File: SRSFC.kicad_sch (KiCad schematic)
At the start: 50 parts, among them J1 SWD_interface, X1 25MHz

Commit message: added servo connectors, schema done (probably)
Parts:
- added J2: POWER, Connector_PinHeader_2.54mm:PinHeader_1x02_P2.54mm_Vertical, symbol Connector_Generic:Conn_01x02
- added J3: SERVO1, Connector_PinHeader_2.54mm:PinHeader_1x03_P2.54mm_Vertical, symbol Connector_Generic:Conn_01x03
- added J4: SERVO2, Connector_PinHeader_2.54mm:PinHeader_1x03_P2.54mm_Vertical, symbol Connector_Generic:Conn_01x03
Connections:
- net +3.3V: now also U6.6 (CSB)
- net GND: now also J2.1 (Pin_1), J3.1 (Pin_1), J4.1 (Pin_1)
- net bmp_scl: now reaches U6.2 (SCK)
- net bmp_sda: now reaches U6.4 (SDI)
- net servo_2: now reaches U1.67 (PA8)
- net servo_2: now also J4.3 (Pin_3)
- net servo_1: now reaches U1.92 (PB6)
- net servo_1: now also J3.3 (Pin_3)
- net +5V renamed VCC
- net VCC: now also J2.2 (Pin_2), J3.2 (Pin_2), J4.2 (Pin_2)
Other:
- moved on the sheet: C1, C10, C11, C12, C13, C14, C15, C16, C17, C18, C19, C2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

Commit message: finished v1 (bad) layout)
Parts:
- C27: value .1uF -> 100nF
- R2: value 1k -> 220
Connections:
- net bmp_scl: now also U1.95 (PB8)
- net bmp_sda: now also U1.93 (PB7)
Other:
- title: (none) -> SRS Flight Computer
- moved on the sheet: C18, C19, C20, C21, C26, J1, R3, R4, R5, R6, U3, U4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
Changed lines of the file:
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@@
 	(generator_version "8.0")
 	(paper "A2")
+	(title_block
+		(title "SRS Flight Computer")
+		(date "2024-11-22")
+		(rev "V1")
+	)

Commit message: updated readme
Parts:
- removed C17, C18, C20: 100nF, Capacitor_SMD:C_0402_1005Metric, symbol Device:C
- removed C19, C21: 1uF, Capacitor_SMD:C_0402_1005Metric, symbol Device:C
- removed U2: ~, ICM-20948:QFN-24_L3.0-W3.0-P0.40-BL-EP, symbol ICM-20948:ICM-20948
- removed U3: ~, TXS0108EPWR:TSSOP-20_L6.5-W4.4-P0.65-LS6.4-BL, symbol TXS0108EPWR:TXS0108EPWR
- removed U4: ~, LP5907MFX-1.8:SOT-23-5_L3.0-W1.7-P0.95-LS2.8-BR, symbol LP5907MFX-1.8:LP5907MFX-1.8/NOPB
- added J5: SERVO3, Connector_PinHeader_2.54mm:PinHeader_1x03_P2.54mm_Vertical, symbol Connector_Generic:Conn_01x03
- added J6: SERVO4, Connector_PinHeader_2.54mm:PinHeader_1x03_P2.54mm_Vertical, symbol Connector_Generic:Conn_01x03
- added J7: SERVO5, Connector_PinHeader_2.54mm:PinHeader_1x03_P2.54mm_Vertical, symbol Connector_Generic:Conn_01x03
- added JP1, JP2: address_select, Jumper:SolderJumper-2_P1.3mm_Open_RoundedPad1.0x1.5mm, symbol Jumper:SolderJumper_2_Open
- added R10, R9: 4.7k, Resistor_SMD:R_0402_1005Metric, symbol Device:R
- added R7, R8: 10k, Resistor_SMD:R_0402_1005Metric, symbol Device:R
- added U2: ~, LSM6DSOWTR:LGA-14L_L3.0-W2.5-P0.50-TL, symbol LSM6DSOWTR:LSM6DSOWTR
- C15: value 1uF -> 100nF
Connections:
- net +3.3V: now also C15.2, C16.1, R10.1, R7.2, R8.2, R9.1, U2.5 (VDDIO), U2.8 (VDD)
- net GND: now also C16.2, J5.1 (Pin_1), J6.1 (Pin_1), J7.1 (Pin_1), JP1.2 (B), JP2.2 (B), U2.2 (SDx), U2.3 (SCx), U2.6 (GND), U2.7 (GND); no longer C16.1
- net VCC: now also J5.2 (Pin_2), J6.2 (Pin_2), J7.2 (Pin_2)
- net bmp_scl: now also R10.2, U2.13 (SCL)
- net bmp_sda: now also R9.2, U2.14 (SDA)
- net at U6.5 (SDO): now also JP2.1 (A)
- net servo_3: now reaches U1.63 (PC6)
- net servo_3: now also J5.3 (Pin_3)
- net servo_4: now reaches U1.64 (PC7)
- net servo_4: now also J6.3 (Pin_3)
- net servo_5: now reaches U1.68 (PA9)
- net servo_5: now also J7.3 (Pin_3)
- removed net +1V8: C15.2, C16.2
- net SPI_CS: no longer names the net of U1.77 (PA15)
- net SPI_MISO: no longer names the net of U1.90 (PB4)
- net SPI_MOSI: no longer names the net of U1.88 (PD7)
- net SPI_SCK: no longer names the net of U1.89 (PB3)
- new net: JP1.1 (A), R8.1, U2.1 (SDO/SA0)
- new net: R7.1, U2.12 (CS)
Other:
- moved on the sheet: J2, J3, J4

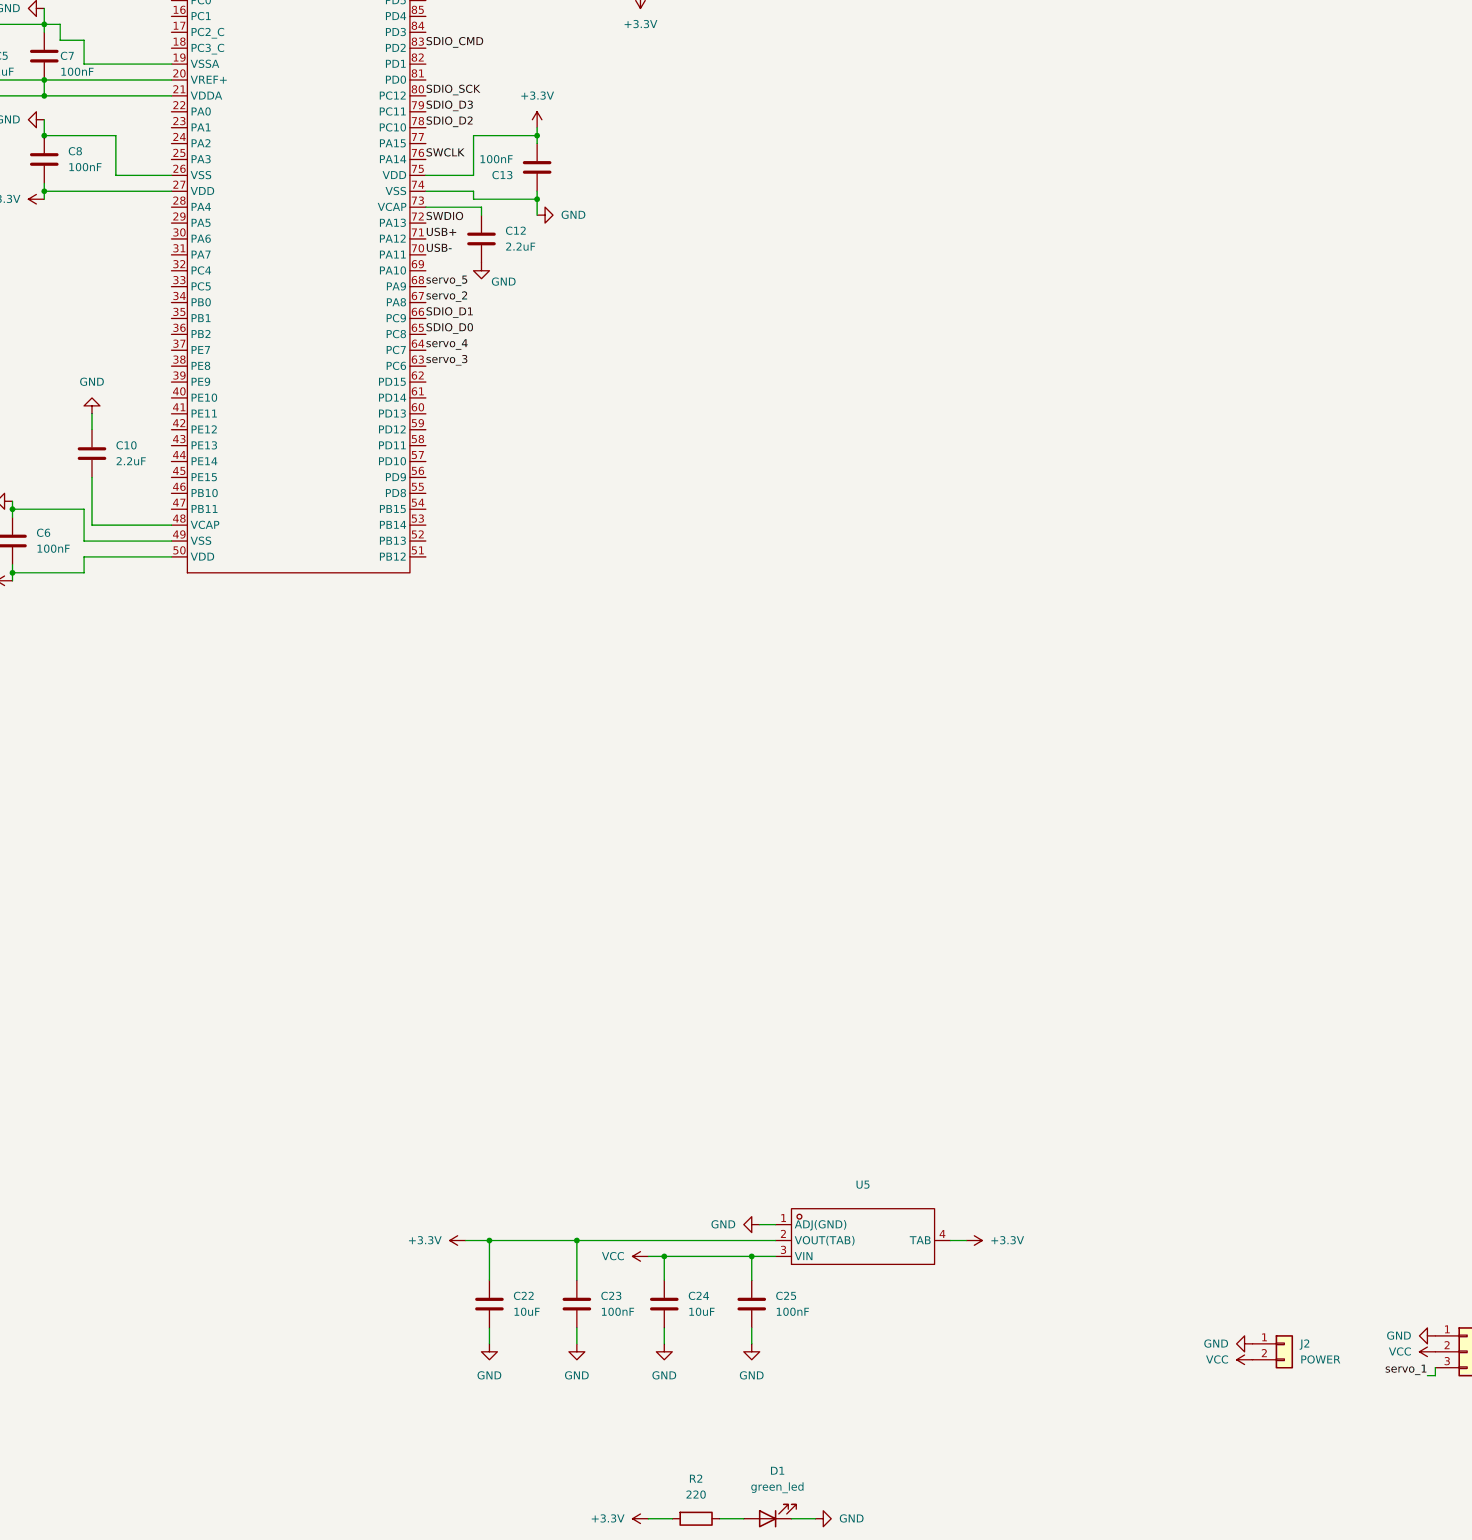
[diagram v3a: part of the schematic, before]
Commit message: added silkscreen, added UART interface
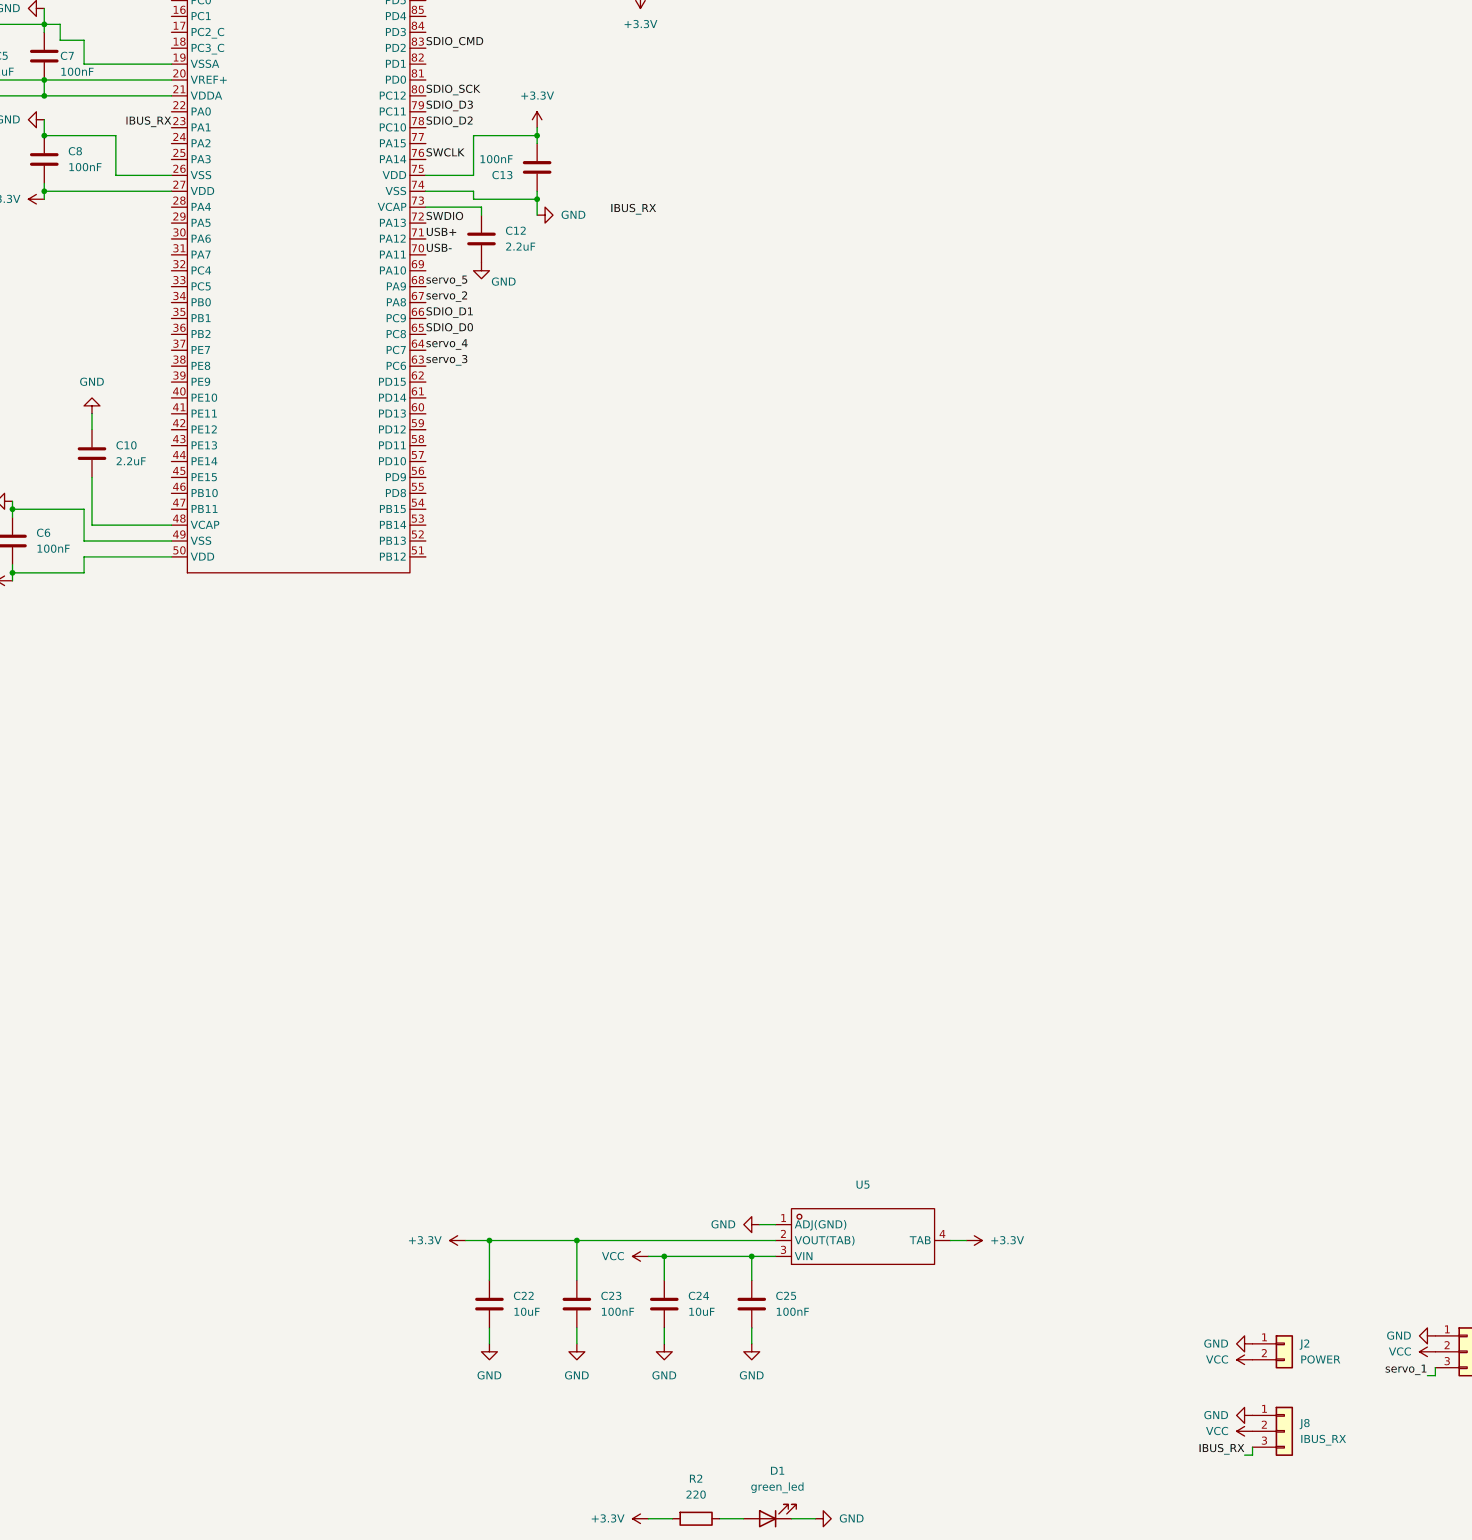
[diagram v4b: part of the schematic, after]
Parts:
- added J8: IBUS_RX, Connector_PinHeader_2.54mm:PinHeader_1x03_P2.54mm_Vertical, symbol Connector_Generic:Conn_01x03
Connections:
- net GND: now also J8.1 (Pin_1)
- net VCC: now also J8.2 (Pin_2)
- net IBUS_RX: now reaches U1.23 (PA1)
- net IBUS_RX: now also J8.3 (Pin_3)

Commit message: changed sensors from i2c to SPI, fixed silkscreen
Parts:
- removed JP1, JP2: address_select, Jumper:SolderJumper-2_P1.3mm_Open_RoundedPad1.0x1.5mm, symbol Jumper:SolderJumper_2_Open
- removed R10, R9: 4.7k, Resistor_SMD:R_0402_1005Metric, symbol Device:R
- removed R7, R8: 10k, Resistor_SMD:R_0402_1005Metric, symbol Device:R
- added C17: 100nF, Capacitor_SMD:C_0402_1005Metric, symbol Device:C
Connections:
- net +3.3V: now also C15.1, C16.2, C17.1; no longer C15.2, C16.1, U6.6 (CSB)
- net GND: now also C15.2, C16.1, C17.2; no longer C15.1, C16.2
- net SPI_MISO_LSM: now reaches U2.1 (SDO/SA0)
- net SPI_MISO_LSM: now also U1.90 (PB4)
- net SPI_CS_LSM: now reaches U2.12 (CS)
- net SPI_CS_LSM: now also U1.88 (PD7)
- net SPI_MISO_BMP: now reaches U6.5 (SDO)
- net SPI_MISO_BMP: now also U1.4 (PE5)
- net SPI_SCK_BMP: now reaches U1.1 (PE2)
- net SPI_SCK_BMP: now also U6.2 (SCK)
- net SPI_CS_BMP: now reaches U1.3 (PE4)
- net SPI_CS_BMP: now also U6.6 (CSB)
- net SPI_MOSI_BMP: now reaches U1.5 (PE6)
- net SPI_MOSI_BMP: now also U6.4 (SDI)
- net SPI_SCK_LSM: now reaches U1.89 (PB3)
- net SPI_SCK_LSM: now also U2.13 (SCL)
- net SPI_MOSI_LSM: now reaches U1.91 (PB5)
- net SPI_MOSI_LSM: now also U2.14 (SDA)
- removed net bmp_scl: U1.95 (PB8), U2.13 (SCL), U6.2 (SCK)
- removed net bmp_sda: U1.93 (PB7), U2.14 (SDA), U6.4 (SDI)
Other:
- moved on the sheet: C11, R1

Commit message: final commit before ordering
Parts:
- R2: value 220 -> 100
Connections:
- net GND: now also CARD1.10, CARD1.11, CARD1.12, CARD1.13, CARD1.6 (VSS); no longer CARD1.CD
- net SDIO_CMD: now also CARD1.3 (CMD); no longer CARD1.6 (VSS)
- net SDIO_D2: now also CARD1.1 (DAT2); no longer CARD1.2 (CD/DAT3)
- net SDIO_D3: now also CARD1.2 (CD/DAT3); no longer CARD1.3 (CMD)
- net SD_CD: now reaches U1.77 (PA15)
- net SD_CD: now also CARD1.CD
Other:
- company: (none) -> avaninder.com
- title: SRS Flight Computer -> Polaris Flight Computer
- moved on the sheet: C27
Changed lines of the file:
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@@
 	(paper "A2")
 	(title_block
-		(title "SRS Flight Computer")
-		(date "2024-11-22")
-		(rev "V1")
+		(title "Polaris Flight Computer")
+		(date "2024-11-29")
+		(rev "V1.0")
+		(company "avaninder.com")
+		(comment 1 "Designed by Avaninder Bhaghayath")
 	)
